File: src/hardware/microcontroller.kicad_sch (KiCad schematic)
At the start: 56 parts, among them J1 Conn_01x02_Pin, J10 Conn_01x04_Pin, J11 Conn_01x04_Pin, J12 Conn_01x02_Pin, J13 Conn_01x02_Pin, J14 Conn_02x08_Top_Bottom, J15 Conn_02x08_Top_Bottom, J16 Conn_02x08_Top_Bottom, J2 Conn_01x02_Pin, J3 Conn_01x02_Pin, J4 Conn_01x02_Pin, J5 Conn_01x02_Pin, J6 Conn_01x04_Pin, J7 Conn_01x04_Pin, J8 Conn_01x04_Pin, J9 Conn_01x04_Pin, U1 SR4W035, U2 NRF54L15-QFAA-R, U3 PCA9306DQER, Y1 ABS07-32.768KHZ-7-T, Y2 ECS-320-8-37B-CKY-TR

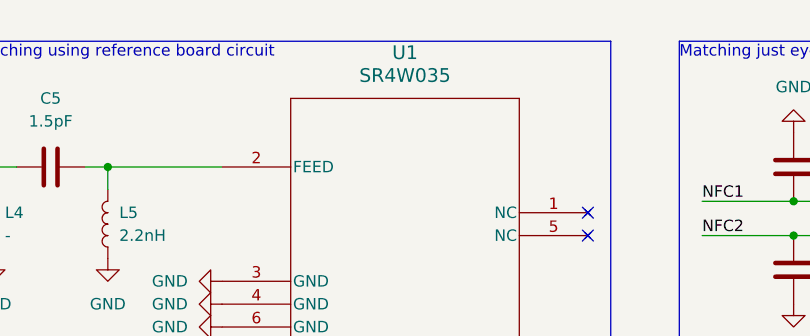
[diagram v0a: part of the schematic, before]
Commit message: Fixed ANT1 Footprint
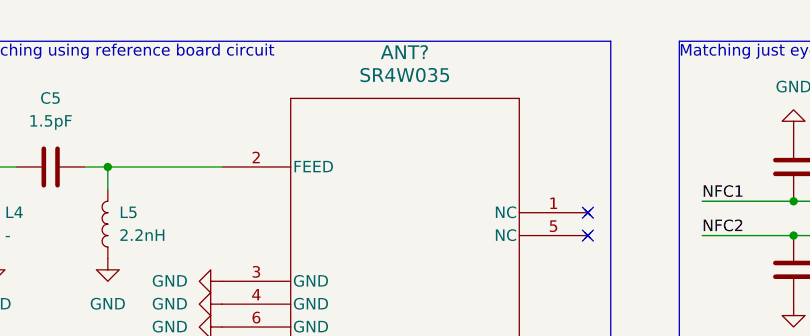
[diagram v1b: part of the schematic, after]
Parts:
- ANT1: footprint Project:WS2816C-1313-4P -> Project:IND_W3102
- renumbered U1 to ANT?
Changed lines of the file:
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@@
 			)
 		)
-		(property "Footprint" "Project:WS2816C-1313-4P"
+		(property "Footprint" "Project:IND_W3102"
 			(at 185.42 40.64 0)
 			(effects
@@
 		(dnp no)
 		(fields_autoplaced yes)
-		(property "Reference" "U1"
+		(property "Reference" "ANT?"
 			(at 128.27 24.13 0)
 			(effects
@@
 			(project "raywatch"
 				(path "/7b654ee8-2a53-4d39-8b7d-32c7bb3cb0ed/fa39c797-7f88-47af-b50c-765e69cbd658"
-					(reference "U1")
+					(reference "ANT?")
 					(unit 1)
 				)

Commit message: Reannotate
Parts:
- gave numbers to parts that had none: 1
- renumbered ANT1 to ANT2, U2 to U1, U3 to U2
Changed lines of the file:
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@@
 		(dnp no)
 		(fields_autoplaced yes)
-		(property "Reference" "ANT1"
+		(property "Reference" "ANT2"
 			(at 187.96 39.3699 90)
 			(effects
@@
 			(project "raywatch"
 				(path "/7b654ee8-2a53-4d39-8b7d-32c7bb3cb0ed/fa39c797-7f88-47af-b50c-765e69cbd658"
-					(reference "ANT1")
+					(reference "ANT2")
 					(unit 1)
 				)
@@
 		(dnp no)
 		(fields_autoplaced yes)
-		(property "Reference" "ANT?"
+		(property "Reference" "ANT1"
 			(at 128.27 24.13 0)
 			(effects
@@
 			(project "raywatch"
 				(path "/7b654ee8-2a53-4d39-8b7d-32c7bb3cb0ed/fa39c797-7f88-47af-b50c-765e69cbd658"
-					(reference "ANT?")
+					(reference "ANT1")
 					(unit 1)
 				)
@@
 		(dnp no)
 		(fields_autoplaced yes)
-		(property "Reference" "U3"
+		(property "Reference" "U2"
 			(at 256.54 21.59 0)
 			(effects
@@
 			(project "raywatch"
 				(path "/7b654ee8-2a53-4d39-8b7d-32c7bb3cb0ed/fa39c797-7f88-47af-b50c-765e69cbd658"
-					(reference "U3")
+					(reference "U2")
 					(unit 1)
 				)
@@
 		(dnp no)
 		(fields_autoplaced yes)
-		(property "Reference" "U2"
+		(property "Reference" "U1"
 			(at 110.49 99.06 0)
 			(effects
@@
 			(project "raywatch"
 				(path "/7b654ee8-2a53-4d39-8b7d-32c7bb3cb0ed/fa39c797-7f88-47af-b50c-765e69cbd658"
-					(reference "U2")
+					(reference "U1")
 					(unit 1)
 				)

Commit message: Changed pin headers to vertical
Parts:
- J1, J12, J13, J2, J3, J4, J5: footprint Connector_PinHeader_2.54mm:PinHeader_1x02_P2.54mm_Horizontal -> Connector_PinHeader_2.54mm:PinHeader_1x02_P2.54mm_Vertical
- J10, J11, J6, J7, J8, J9: footprint Connector_PinHeader_2.54mm:PinHeader_1x04_P2.54mm_Horizontal -> Connector_PinHeader_2.54mm:PinHeader_1x04_P2.54mm_Vertical
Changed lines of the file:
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@@
 			)
 		)
-		(property "Footprint" "Connector_PinHeader_2.54mm:PinHeader_1x04_P2.54mm_Horizontal"
+		(property "Footprint" "Connector_PinHeader_2.54mm:PinHeader_1x04_P2.54mm_Vertical"
 			(at 45.72 137.16 0)
 			(effects
@@
 			)
 		)
-		(property "Footprint" "Connector_PinHeader_2.54mm:PinHeader_1x04_P2.54mm_Horizontal"
+		(property "Footprint" "Connector_PinHeader_2.54mm:PinHeader_1x04_P2.54mm_Vertical"
 			(at 48.26 167.64 0)
 			(effects
@@
 			)
 		)
-		(property "Footprint" "Connector_PinHeader_2.54mm:PinHeader_1x02_P2.54mm_Horizontal"
+		(property "Footprint" "Connector_PinHeader_2.54mm:PinHeader_1x02_P2.54mm_Vertical"
 			(at 205.74 157.48 0)
 			(effects
@@
 			)
 		)
-		(property "Footprint" "Connector_PinHeader_2.54mm:PinHeader_1x04_P2.54mm_Horizontal"
+		(property "Footprint" "Connector_PinHeader_2.54mm:PinHeader_1x04_P2.54mm_Vertical"
 			(at 156.21 129.54 0)
 			(effects
@@
 			)
 		)
-		(property "Footprint" "Connector_PinHeader_2.54mm:PinHeader_1x02_P2.54mm_Horizontal"
+		(property "Footprint" "Connector_PinHeader_2.54mm:PinHeader_1x02_P2.54mm_Vertical"
 			(at 26.67 124.46 0)
 			(effects
@@
 			)
 		)
-		(property "Footprint" "Connector_PinHeader_2.54mm:PinHeader_1x02_P2.54mm_Horizontal"
+		(property "Footprint" "Connector_PinHeader_2.54mm:PinHeader_1x02_P2.54mm_Vertical"
 			(at 33.02 74.93 0)
 			(effects
@@
 			)
 		)
-		(property "Footprint" "Connector_PinHeader_2.54mm:PinHeader_1x04_P2.54mm_Horizontal"
+		(property "Footprint" "Connector_PinHeader_2.54mm:PinHeader_1x04_P2.54mm_Vertical"
 			(at 173.99 157.48 0)
 			(effects
@@
 			)
 		)
-		(property "Footprint" "Connector_PinHeader_2.54mm:PinHeader_1x02_P2.54mm_Horizontal"
+		(property "Footprint" "Connector_PinHeader_2.54mm:PinHeader_1x02_P2.54mm_Vertical"
 			(at 195.58 142.24 0)
 			(effects
@@
 			)
 		)
-		(property "Footprint" "Connector_PinHeader_2.54mm:PinHeader_1x04_P2.54mm_Horizontal"
+		(property "Footprint" "Connector_PinHeader_2.54mm:PinHeader_1x04_P2.54mm_Vertical"
 			(at 156.21 147.32 0)
 			(effects
@@
 			)
 		)
-		(property "Footprint" "Connector_PinHeader_2.54mm:PinHeader_1x02_P2.54mm_Horizontal"
+		(property "Footprint" "Connector_PinHeader_2.54mm:PinHeader_1x02_P2.54mm_Vertical"
 			(at 29.21 161.29 0)
 			(effects
@@
 			)
 		)
-		(property "Footprint" "Connector_PinHeader_2.54mm:PinHeader_1x02_P2.54mm_Horizontal"
+		(property "Footprint" "Connector_PinHeader_2.54mm:PinHeader_1x02_P2.54mm_Vertical"
 			(at 36.83 60.96 0)
 			(effects
@@
 			)
 		)
-		(property "Footprint" "Connector_PinHeader_2.54mm:PinHeader_1x04_P2.54mm_Horizontal"
+		(property "Footprint" "Connector_PinHeader_2.54mm:PinHeader_1x04_P2.54mm_Vertical"
 			(at 156.21 162.56 0)
 			(effects
@@
 			)
 		)
-		(property "Footprint" "Connector_PinHeader_2.54mm:PinHeader_1x02_P2.54mm_Horizontal"
+		(property "Footprint" "Connector_PinHeader_2.54mm:PinHeader_1x02_P2.54mm_Vertical"
 			(at 35.56 119.38 0)
 			(effects

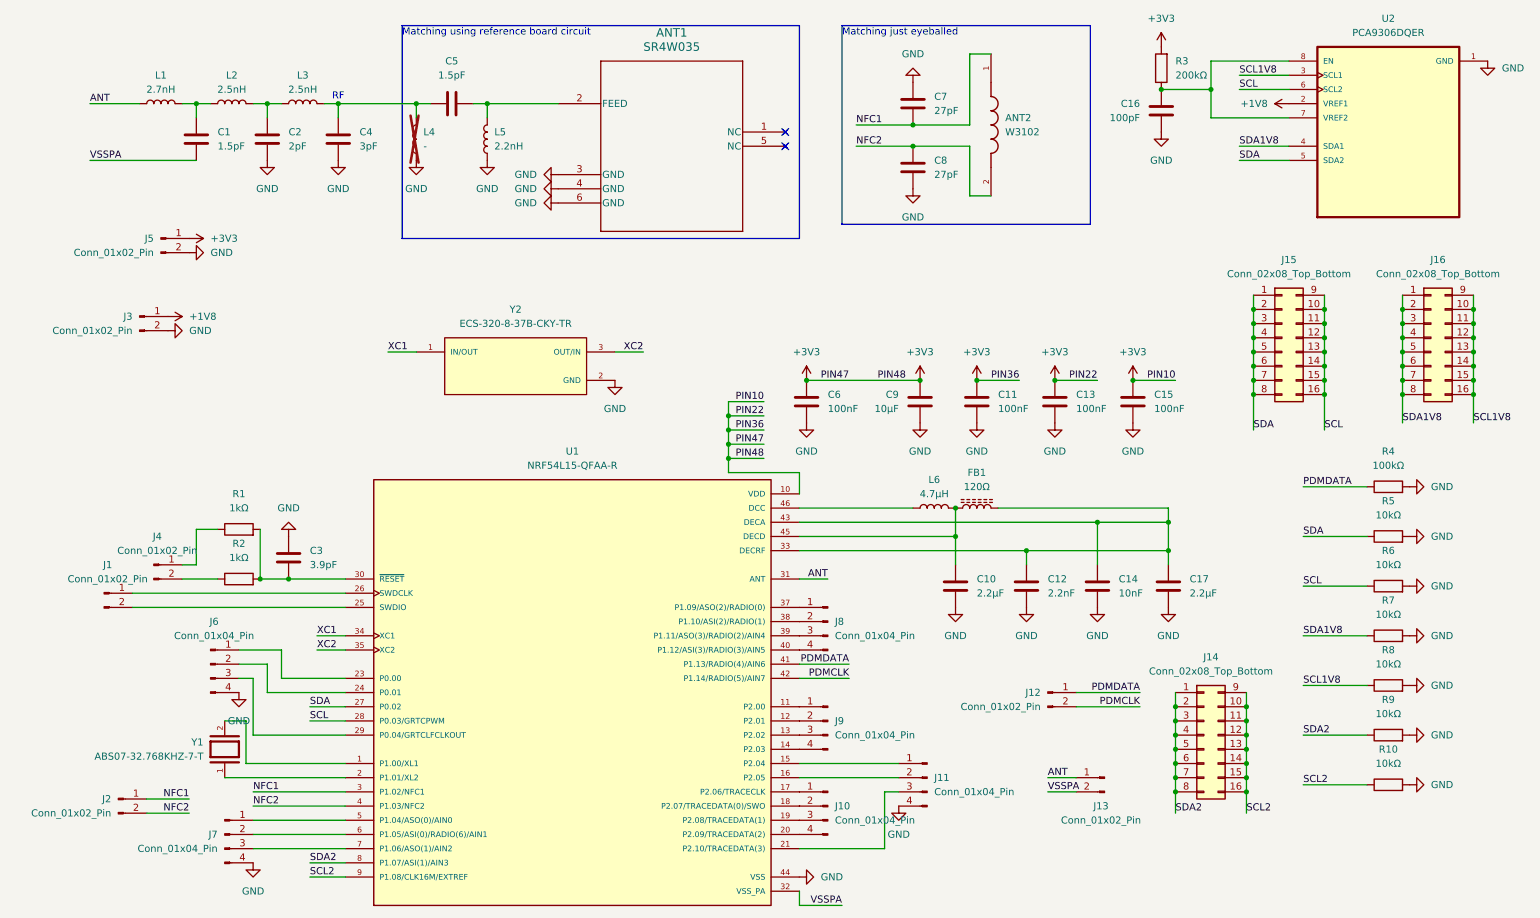
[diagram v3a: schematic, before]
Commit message: Fixed connector footprints; Changed conectors from 2.54 to 1.27
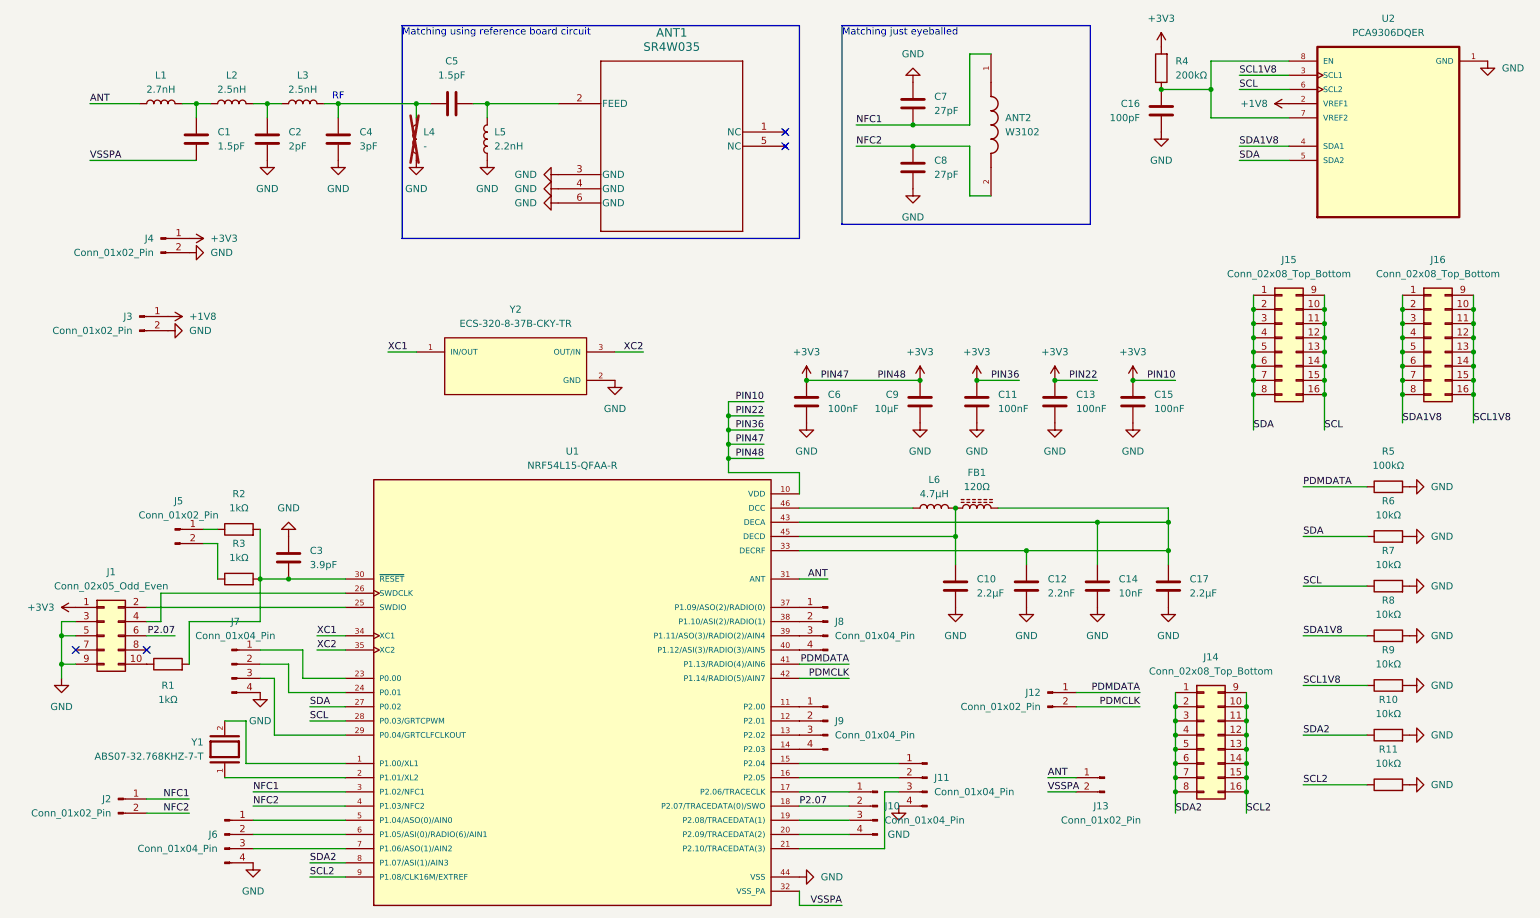
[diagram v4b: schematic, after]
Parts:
- removed J1: Conn_01x02_Pin, Connector_PinHeader_2.54mm:PinHeader_1x02_P2.54mm_Vertical, symbol Connector:Conn_01x02_Pin
- added J1: Conn_02x05_Odd_Even, Connector_PinHeader_1.27mm:PinHeader_2x05_P1.27mm_Vertical, symbol Connector_Generic:Conn_02x05_Odd_Even
- added R1: 1kΩ, Resistor_SMD:R_0402_1005Metric, symbol Device:R
- J10, J11, J8, J9: footprint Connector_PinHeader_2.54mm:PinHeader_1x04_P2.54mm_Vertical -> Connector_PinHeader_1.27mm:PinHeader_1x04_P1.27mm_Vertical
- J12, J13, J2, J3: footprint Connector_PinHeader_2.54mm:PinHeader_1x02_P2.54mm_Vertical -> Connector_PinHeader_1.27mm:PinHeader_1x02_P1.27mm_Vertical
- J14, J15, J16: footprint Connector_PinHeader_2.54mm:PinHeader_2x08_P2.54mm_Vertical -> Connector_PinHeader_1.27mm:PinHeader_2x08_P1.27mm_Vertical
- J4: renamed from J5; footprint Connector_PinHeader_2.54mm:PinHeader_1x02_P2.54mm_Vertical -> Connector_PinHeader_1.27mm:PinHeader_1x02_P1.27mm_Vertical
- J5: renamed from J4; footprint Connector_PinHeader_2.54mm:PinHeader_1x02_P2.54mm_Vertical -> Connector_PinHeader_1.27mm:PinHeader_1x02_P1.27mm_Vertical
- J6: renamed from J7; footprint Connector_PinHeader_2.54mm:PinHeader_1x04_P2.54mm_Vertical -> Connector_PinHeader_1.27mm:PinHeader_1x04_P1.27mm_Vertical
- J7: renamed from J6; footprint Connector_PinHeader_2.54mm:PinHeader_1x04_P2.54mm_Vertical -> Connector_PinHeader_1.27mm:PinHeader_1x04_P1.27mm_Vertical
- renumbered R9 to R10, R10 to R11, R1 to R2, R2 to R3, R3 to R4, R4 to R5, R5 to R6, R6 to R7, R7 to R8, R8 to R9
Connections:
- net +3V3: now also J1.1 (Pin_1)
- net GND: now also J1.3 (Pin_3), J1.5 (Pin_5), J1.9 (Pin_9)
- net at C3.2, R2.2, R3.2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: now also R1.2
- net at U1.26 (SWDCLK): now also J1.4 (Pin_4)
- net at U1.25 (SWDIO): now also J1.2 (Pin_2)
- net P2.07: now reaches J10.2 (Pin_2), U1.18 (P2.07/TRACEDATA(0)/SWO)
- net P2.07: now also J1.6 (Pin_6)
- new net: J1.10 (Pin_10), R1.1
- no-connect marks 2 -> 4
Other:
- moved on the sheet: J10, J5, J7

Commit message: Fixes; Added TPM PCB
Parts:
- C1, C10, C11, C12, C13, C14, C15, C16, C17, C2, C3, C4, C5, C6, C7, C8, C9: footprint Capacitor_SMD:C_0504_1310Metric -> Capacitor_SMD:C_0402_1005Metric
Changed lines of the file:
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@@
 			)
 		)
-		(property "Footprint" "Capacitor_SMD:C_0504_1310Metric"
+		(property "Footprint" "Capacitor_SMD:C_0402_1005Metric"
 			(at 54.9148 46.99 0)
 			(effects
@@
 			)
 		)
-		(property "Footprint" "Capacitor_SMD:C_0504_1310Metric"
+		(property "Footprint" "Capacitor_SMD:C_0402_1005Metric"
 			(at 60.6552 121.92 0)
 			(effects
@@
 			)
 		)
-		(property "Footprint" "Capacitor_SMD:C_0504_1310Metric"
+		(property "Footprint" "Capacitor_SMD:C_0402_1005Metric"
 			(at 172.4152 40.64 0)
 			(effects
@@
 			)
 		)
-		(property "Footprint" "Capacitor_SMD:C_0504_1310Metric"
+		(property "Footprint" "Capacitor_SMD:C_0402_1005Metric"
 			(at 171.7548 93.98 0)
 			(effects
@@
 			)
 		)
-		(property "Footprint" "Capacitor_SMD:C_0504_1310Metric"
+		(property "Footprint" "Capacitor_SMD:C_0402_1005Metric"
 			(at 216.2048 127 0)
 			(effects
@@
 			)
 		)
-		(property "Footprint" "Capacitor_SMD:C_0504_1310Metric"
+		(property "Footprint" "Capacitor_SMD:C_0402_1005Metric"
 			(at 190.8048 127 0)
 			(effects
@@
 			)
 		)
-		(property "Footprint" "Capacitor_SMD:C_0504_1310Metric"
+		(property "Footprint" "Capacitor_SMD:C_0402_1005Metric"
 			(at 153.3652 93.98 0)
 			(effects
@@
 			)
 		)
-		(property "Footprint" "Capacitor_SMD:C_0504_1310Metric"
+		(property "Footprint" "Capacitor_SMD:C_0402_1005Metric"
 			(at 42.2148 46.99 0)
 			(effects
@@
 			)
 		)
-		(property "Footprint" "Capacitor_SMD:C_0504_1310Metric"
+		(property "Footprint" "Capacitor_SMD:C_0402_1005Metric"
 			(at 178.1048 127 0)
 			(effects
@@
 			)
 		)
-		(property "Footprint" "Capacitor_SMD:C_0504_1310Metric"
+		(property "Footprint" "Capacitor_SMD:C_0402_1005Metric"
 			(at 203.5048 127 0)
 			(effects
@@
 			)
 		)
-		(property "Footprint" "Capacitor_SMD:C_0504_1310Metric"
+		(property "Footprint" "Capacitor_SMD:C_0402_1005Metric"
 			(at 172.4152 52.07 0)
 			(effects
@@
 			)
 		)
-		(property "Footprint" "Capacitor_SMD:C_0504_1310Metric"
+		(property "Footprint" "Capacitor_SMD:C_0402_1005Metric"
 			(at 216.8652 41.91 0)
 			(effects
@@
 			)
 		)
-		(property "Footprint" "Capacitor_SMD:C_0504_1310Metric"
+		(property "Footprint" "Capacitor_SMD:C_0402_1005Metric"
 			(at 92.71 37.7952 0)
 			(effects
@@
 			)
 		)
-		(property "Footprint" "Capacitor_SMD:C_0504_1310Metric"
+		(property "Footprint" "Capacitor_SMD:C_0402_1005Metric"
 			(at 181.9148 86.36 0)
 			(effects
@@
 			)
 		)
-		(property "Footprint" "Capacitor_SMD:C_0504_1310Metric"
+		(property "Footprint" "Capacitor_SMD:C_0402_1005Metric"
 			(at 195.8848 86.36 0)
 			(effects
@@
 			)
 		)
-		(property "Footprint" "Capacitor_SMD:C_0504_1310Metric"
+		(property "Footprint" "Capacitor_SMD:C_0402_1005Metric"
 			(at 67.6148 46.99 0)
 			(effects
@@
 			)
 		)
-		(property "Footprint" "Capacitor_SMD:C_0504_1310Metric"
+		(property "Footprint" "Capacitor_SMD:C_0402_1005Metric"
 			(at 209.8548 93.98 0)
 			(effects

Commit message: Fixed 02x08 connector symbol
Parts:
- removed J14, J15, J16: Conn_02x08_Top_Bottom, Connector_PinHeader_1.27mm:PinHeader_2x08_P1.27mm_Vertical, symbol Connector_Generic:Conn_02x08_Top_Bottom
- added J14, J15, J16: Conn_02x08_Odd_Even, symbol Connector_Generic:Conn_02x08_Odd_Even
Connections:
- net SCL: now also J15.10 (Pin_10), J15.12 (Pin_12), J15.14 (Pin_14), J15.16 (Pin_16), J15.2 (Pin_2), J15.4 (Pin_4), J15.6 (Pin_6), J15.8 (Pin_8)
- net SCL1V8: now also J16.10 (Pin_10), J16.12 (Pin_12), J16.14 (Pin_14), J16.16 (Pin_16), J16.2 (Pin_2), J16.4 (Pin_4), J16.6 (Pin_6), J16.8 (Pin_8)
- net SCL2: now also J14.10 (Pin_10), J14.12 (Pin_12), J14.14 (Pin_14), J14.16 (Pin_16), J14.2 (Pin_2), J14.4 (Pin_4), J14.6 (Pin_6), J14.8 (Pin_8)
- net SDA: now also J15.1 (Pin_1), J15.11 (Pin_11), J15.13 (Pin_13), J15.15 (Pin_15), J15.3 (Pin_3), J15.5 (Pin_5), J15.7 (Pin_7), J15.9 (Pin_9)
- net SDA1V8: now also J16.1 (Pin_1), J16.11 (Pin_11), J16.13 (Pin_13), J16.15 (Pin_15), J16.3 (Pin_3), J16.5 (Pin_5), J16.7 (Pin_7), J16.9 (Pin_9)
- net SDA2: now also J14.1 (Pin_1), J14.11 (Pin_11), J14.13 (Pin_13), J14.15 (Pin_15), J14.3 (Pin_3), J14.5 (Pin_5), J14.7 (Pin_7), J14.9 (Pin_9)

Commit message: Applied fixes
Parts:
- J14, J15, J16: footprint (none) -> Connector_PinHeader_1.27mm:PinHeader_2x08_P1.27mm_Vertical
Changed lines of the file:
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@@
 			)
 		)
-		(property "Footprint" ""
+		(property "Footprint" "Connector_PinHeader_1.27mm:PinHeader_2x08_P1.27mm_Vertical"
 			(at 223.52 149.86 0)
 			(effects
@@
 			)
 		)
-		(property "Footprint" ""
+		(property "Footprint" "Connector_PinHeader_1.27mm:PinHeader_2x08_P1.27mm_Vertical"
 			(at 237.49 78.74 0)
 			(effects
@@
 			)
 		)
-		(property "Footprint" ""
+		(property "Footprint" "Connector_PinHeader_1.27mm:PinHeader_2x08_P1.27mm_Vertical"
 			(at 264.16 78.74 0)
 			(effects
